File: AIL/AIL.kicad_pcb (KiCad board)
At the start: 2 copper layers, 115.5 x 48.6 mm, 30 parts, among them J1 Screw_Terminal_01x02, J2 Screw_Terminal_01x02, Q1 BC548, U1 TPL290

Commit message: review das placas
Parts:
- added G***: UFRGS_14.7x8.0mm_Copper, e-Power:Logo_UFRGS_14.7x8.0mm_SilkS, F.Cu at (89.9, 128.0)

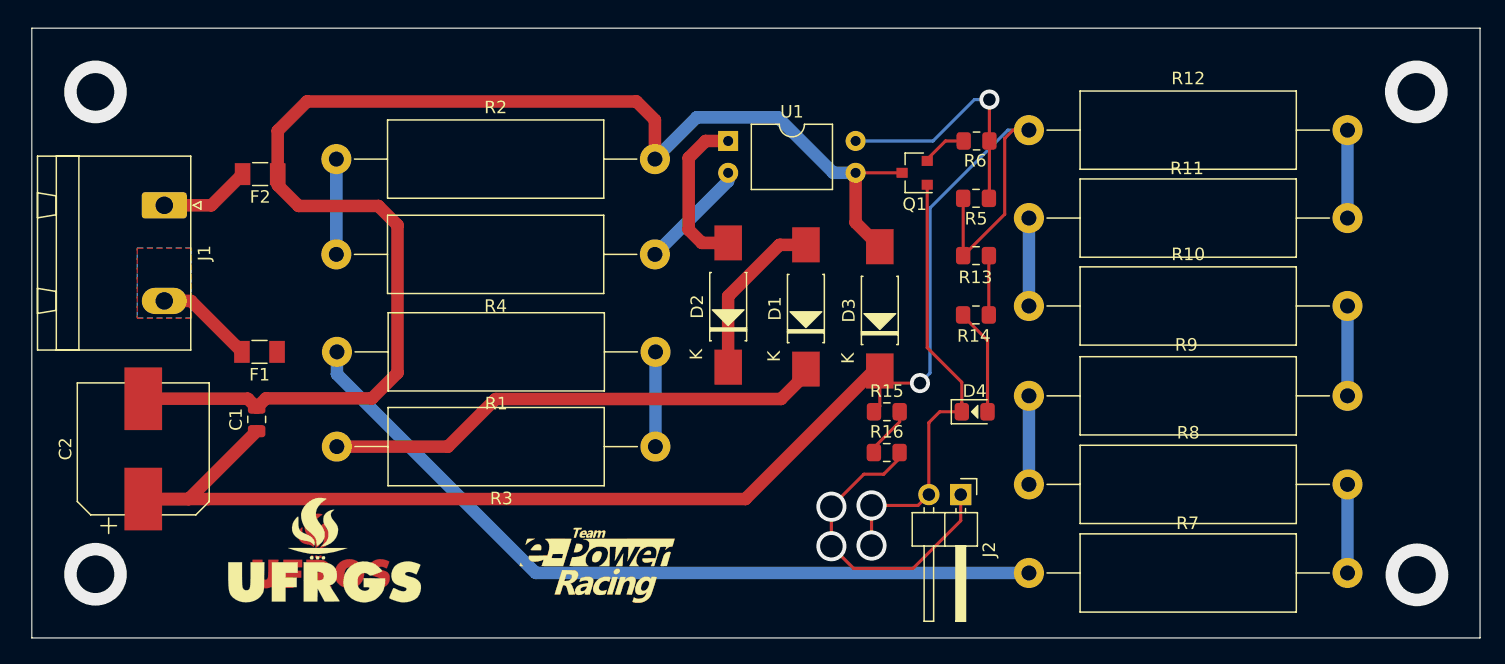
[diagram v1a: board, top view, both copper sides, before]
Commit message: AIL schematic and layout att. BSPD layout att.
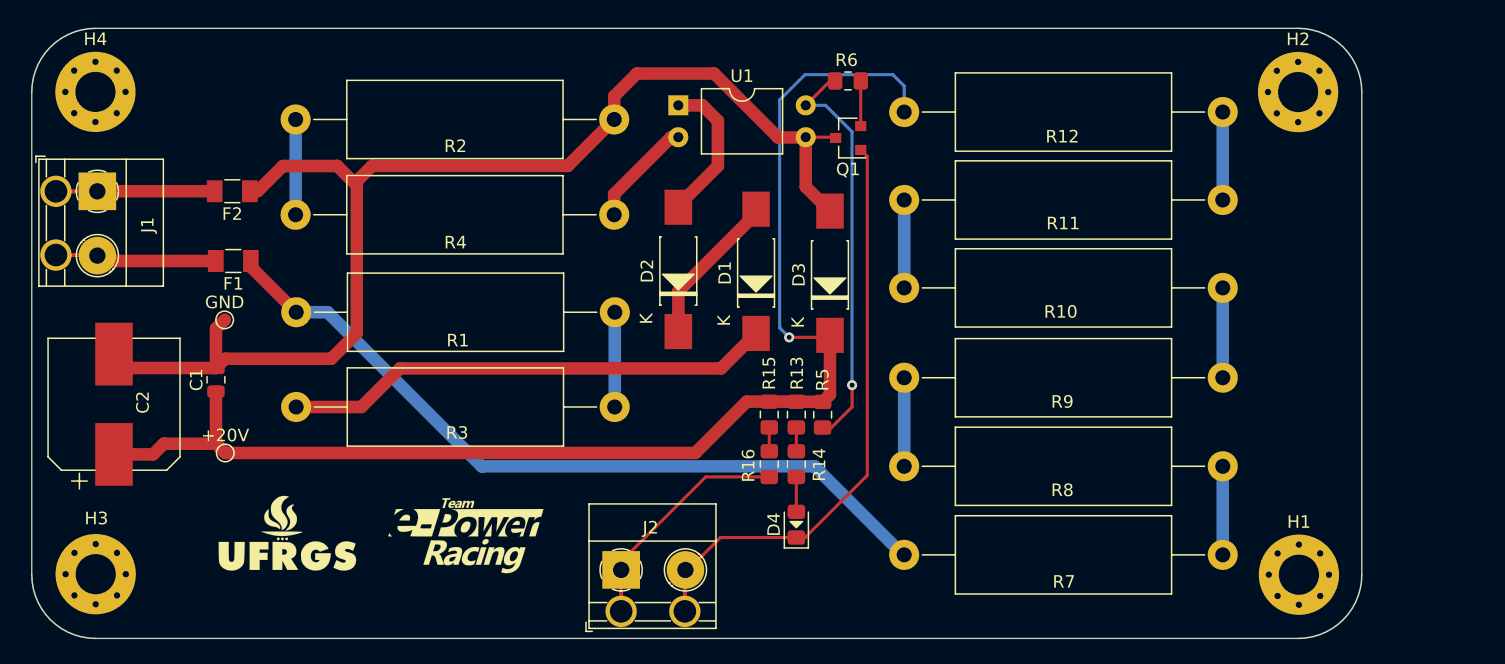
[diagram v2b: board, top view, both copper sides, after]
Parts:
- removed G***: UFRGS_14.7x8.0mm_Copper, e-Power:Logo_UFRGS_14.7x8.0mm_SilkS
- added H1: NC, e-Power:MountingHole_3.2mm_M3_Pad_Via, F.Cu at (167.6, 130.0)
- added H2: NC, e-Power:MountingHole_3.2mm_M3_Pad_Via, F.Cu at (167.5, 91.5)
- added H3: NC, e-Power:MountingHole_3.2mm_M3_Pad_Via, F.Cu at (71.6, 129.9)
- added H4: NC, e-Power:MountingHole_3.2mm_M3_Pad_Via, F.Cu at (71.6, 91.5)
- added TP1: +20V, e-Power:TestPoint_Pad_D1.0mm, F.Cu at (82.0, 120.3)
- added TP2: GND, e-Power:TestPoint_Pad_D1.0mm, F.Cu at (81.9, 109.7)
- G1: footprint e-Power:e-Power_12.4x6.0mm_Copper -> e-Power:Logo_e-Power_12.4x6.0mm_SilkS
- G2: footprint e-Power:UFRGS_11.0x6.0mm_Copper -> e-Power:Logo_UFRGS_11.0x6.0mm_SilkS
- J1: footprint Connector_Phoenix_GMSTB:PhoenixContact_GMSTBA_2,5_2-G-7,62_1x02_P7.62mm_Horizontal -> e-Power:TerminalBlock_Phoenix_MKDS-1,5-2_1x02_P5.08mm_Horizontal
- J2: footprint Connector_PinHeader_2.54mm:PinHeader_1x02_P2.54mm_Horizontal -> e-Power:TerminalBlock_Phoenix_MKDS-1,5-2_1x02_P5.08mm_Horizontal
- moved J2 27.7 mm to (113.5, 129.6), turned to 0 degrees
- moved R5 21.2 mm to (129.6, 117.2), turned to 270 degrees
- moved R13 19.1 mm to (127.5, 117.2), turned to 270 degrees
- moved R14 18.6 mm to (127.5, 121.2), turned to 270 degrees
- moved D4 16.8 mm to (127.5, 126.0), turned to 90 degrees
- moved R6 11.3 mm to (131.6, 90.6), turned to 180 degrees
- moved G1 10.7 mm to (101.1, 126.9)
- moved R10 10.0 mm to (136.1, 107.1)
- moved R8 10.0 mm to (136.1, 121.3)
- moved R12 10.0 mm to (136.1, 93.1)
- moved R11 10.0 mm to (161.5, 100.1)
- moved R9 10.0 mm to (161.5, 114.3)
- moved R7 10.0 mm to (161.5, 128.4)
- moved R16 9.41 mm to (125.3, 121.2), turned to 270 degrees
- moved R15 9.38 mm to (125.3, 117.2), turned to 270 degrees
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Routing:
- net +20V: track 123.5 -> 106.2 mm
- net GND: track 113.1 -> 98.9 mm
- net Net-(R5-Pad2): track 19.9 -> 32.7 mm
- net Net-(J2-Pad1): track 25.4 -> 15.1 mm, vias 2 -> 0
- net Net-(D4-Pad1): track 36.1 -> 43.5 mm, vias 2 -> 0
- net Net-(D4-Pad2): track 8.53 -> 2.78 mm
- net Net-(R13-Pad2): track 4.73 -> 1.90 mm
- net Net-(R15-Pad2): track 4.10 -> 1.91 mm
- net Net-(F2-Pad2): track 7.27 -> 9.00 mm
- net Net-(F1-Pad2): track 7.87 -> 9.60 mm
- net /TS+: track 63.5 -> 62.2 mm
- net Net-(D1-Pad2): track 13.6 -> 12.3 mm
- net Net-(D2-Pad2): track 13.0 -> 11.9 mm
- net Net-(D1-Pad1): track 40.2 -> 39.1 mm
- net (no net): vias 4 -> 0
- removed copper zone on B.Cu, net (none)
- removed copper zone on F.Cu, net (none)
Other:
- board size 115.5 x 48.6 mm -> 106 x 48.6 mm

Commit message: att set/reset and ail 07/09/2020
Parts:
- C2: footprint e-Power:CP_Elec_10x10 -> Capacitor_SMD:CP_Elec_8x10
- D1, D2, D3: footprint e-Power:DO-41_SMD -> e-Power:DO-35_SMD
- G1: value e-Power_12.4x6.0mm_Copper -> Logo_e-Power_Large; footprint e-Power:Logo_e-Power_12.4x6.0mm_SilkS -> e-Power:Logo_e-Power_16.5x8.0mm_SilkS
- G2: value UFRGS_1_11.0x6.0mm_Copper -> Logo_UFRGS_Large; footprint e-Power:Logo_UFRGS_11.0x6.0mm_SilkS -> e-Power:Logo_UFRGS_14.7x8.0mm_SilkS
- moved J2 3.05 mm to (116.6, 129.5)
- moved C2 2.82 mm to (72.8, 113.6)
- moved G1 2.04 mm to (101.4, 128.9)
- moved G2 1.58 mm to (84.9, 127.4)
- moved D3 1.01 mm to (129.2, 109.8)
- moved D1 0.55 mm to (123.7, 109.7)
- moved D2 0.40 mm to (118.4, 109.9)
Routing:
- net Net-(F2-Pad2): track 9.00 -> 12.7 mm
- net Net-(F1-Pad2): track 9.60 -> 12.9 mm
- net +20V: track 106.2 -> 103.5 mm
- net Net-(D2-Pad2): track 11.9 -> 10.4 mm
- net Net-(D1-Pad1): track 39.1 -> 40.2 mm
- net Net-(J2-Pad1): track 15.1 -> 16.1 mm
- net GND: track 98.9 -> 97.9 mm
- net Net-(D4-Pad1): track 43.5 -> 44.0 mm

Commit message: geretate BSPD gerbers
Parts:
- moved C2 2.83 mm to (72.1, 116.3)
- moved D3 0.72 mm to (128.7, 109.3)
- moved F2 0.72 mm to (82.0, 98.9)
- moved R11 0.72 mm to (161.0, 99.6)
- moved R15 0.72 mm to (124.8, 116.7)
- moved R3 0.72 mm to (87.1, 116.1)
- moved R5 0.72 mm to (129.1, 116.7)
- moved R6 0.72 mm to (131.1, 90.1)
- moved R7 0.72 mm to (161.0, 127.9)
- moved TP1 0.72 mm to (81.5, 119.8)
- moved D1 0.72 mm to (123.2, 109.2)
- moved D2 0.72 mm to (117.9, 109.4)
- moved F1 0.72 mm to (82.1, 104.5)
- moved G1 0.72 mm to (100.9, 128.4)
- moved G2 0.72 mm to (84.4, 126.8)
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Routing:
- net +20V: track 103.5 -> 105.1 mm
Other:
- board size 106 x 48.6 mm -> 106.7 x 48.3 mm
- board text added: "> AIL"
- board text added: "> Leonardo Motta"
- board text added: "> Rev. A | 18.09.2020"
- board text added: "> e-Power UFRGS"
- board text added: "A"
- board text added: "K"
- board text added: "TESTED"
- board text added: "TS+"
- board text added: "TS-"

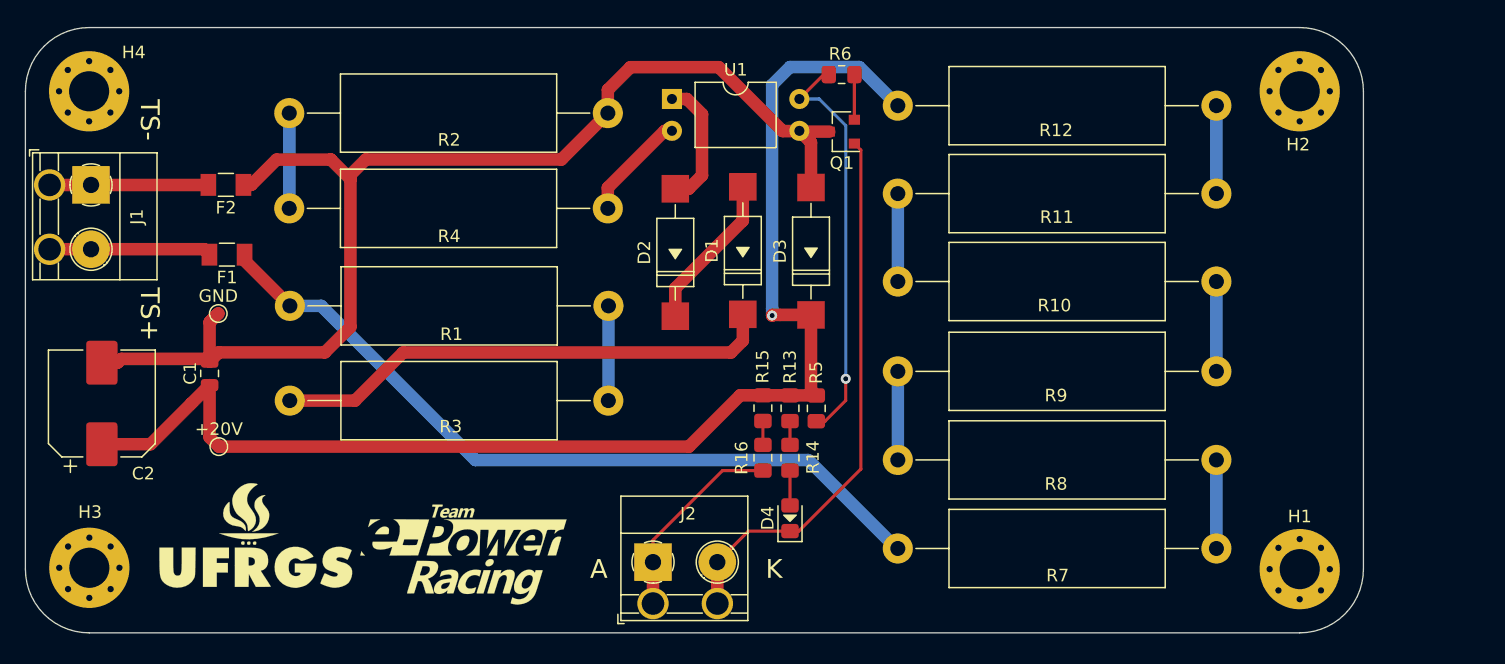
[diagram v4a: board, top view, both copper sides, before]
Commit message: dimenssion AIL
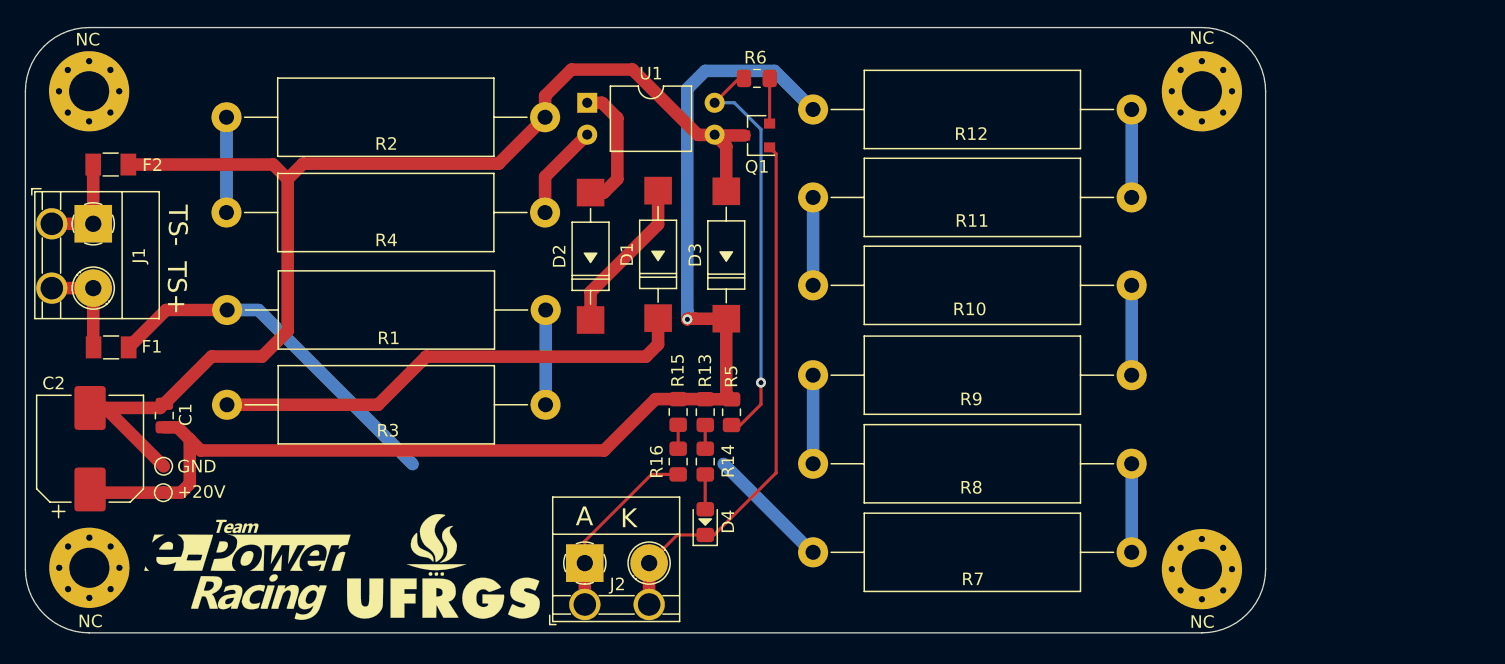
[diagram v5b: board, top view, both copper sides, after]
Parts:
- moved G1 17.3 mm to (83.7, 129.6)
- moved G2 15.2 mm to (99.4, 129.3)
- moved TP2 12.9 mm to (77.1, 121.3)
- moved F1 11.8 mm to (72.9, 111.9)
- moved F2 9.32 mm to (72.8, 97.3)
- moved NC 7.80 mm to (159.8, 129.5)
- moved NC 7.80 mm to (159.8, 91.4)
- moved R10 6.76 mm to (128.8, 106.9)
- moved R12 6.76 mm to (128.8, 92.9)
- moved R8 6.76 mm to (128.8, 121.1)
- moved D1 6.76 mm to (116.5, 109.5)
- moved D2 6.76 mm to (111.1, 109.7)
- moved D3 6.76 mm to (121.9, 109.6)
- moved D4 6.76 mm to (120.2, 125.8)
- moved Q1 6.76 mm to (124.4, 95.0)
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- renumbered H1 to NC, H2 to NC, H3 to NC, H4 to NC
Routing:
- net /TS+: track 62.2 -> 39.2 mm
- net +20V: track 105.1 -> 99.6 mm
- net Net-(F1-Pad2): track 12.9 -> 8.04 mm
- net Net-(F2-Pad2): track 12.7 -> 8.03 mm
- net Net-(D1-Pad1): track 40.2 -> 38.5 mm
- net Net-(D4-Pad1): track 44.0 -> 42.6 mm
- net Net-(J2-Pad1): track 16.1 -> 14.7 mm
- net GND: track 98.3 -> 99.6 mm
- net Net-(R4-Pad1): track 8.64 -> 7.60 mm
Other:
- board size 106.7 x 48.3 mm -> 98.9 x 48.3 mm

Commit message: AIL atualizado
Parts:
- removed R5: 10K, Resistor_SMD:R_0805_2012Metric_Pad1.15x1.40mm_HandSolder
- Q1: value BC548 -> BC807; footprint e-Power:SOT-23 -> Package_TO_SOT_SMD:SOT-23
- moved Q1 18.1 mm to (123.0, 113.0), turned to 270 degrees
- moved D4 2.19 mm to (120.2, 128.0)
- moved R6 1.59 mm to (124.4, 92.0)
- moved J2 0.28 mm to (110.4, 129.0)
- renumbered NC to H1, NC to H2, NC to H3, NC to H4
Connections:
- D4 pad 1: Net-(D4-Pad1) -> GND
- J2 pad 2: Net-(D4-Pad1) -> GND
- Q1 pad 1: Net-(D4-Pad1) -> Net-(Q1-Pad1)
- Q1 pad 2: Net-(Q1-Pad2) -> +20V
- Q1 pad 3: GND -> Net-(Q1-Pad3)
- R13 pad 1: +20V -> Net-(Q1-Pad3)
- R15 pad 1: +20V -> Net-(Q1-Pad3)
- R6 pad 1: Net-(Q1-Pad2) -> Net-(Q1-Pad1)
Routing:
- net Net-(D4-Pad1): track 42.6 -> 0.00 mm
- net GND: track 99.6 -> 139.8 mm, vias 0 -> 1
- net Net-(R5-Pad2): track 32.7 -> 2.49 mm, vias 1 -> 0
- net /TS+: track 39.2 -> 64.0 mm
- net Net-(Q1-Pad1): track 0.00 -> 21.9 mm
- net +20V: track 99.6 -> 86.0 mm
- net Net-(Q1-Pad3): track 0.00 -> 5.74 mm
- net Net-(Q1-Pad2): track 3.60 -> 0.00 mm
- net Net-(D4-Pad2): track 2.78 -> 5.73 mm
